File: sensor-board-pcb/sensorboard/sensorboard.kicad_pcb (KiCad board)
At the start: 2 copper layers, 19 parts, among them J1 TO_MOTHERBOARD, J10 PZT_08, J11 PZT_09, J12 PZT_10, J13 PZT_11, J14 PZT_12, J15 PZT_13, J16 PZT_14, J17 PZT_15, J2 PZT_00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

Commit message: board
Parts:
- moved J4 255.7 mm to (113.0, 129.0)
- moved J3 252.5 mm to (113.0, 119.2)
- moved J2 249.8 mm to (113.0, 108.7)
- moved J12 248.5 mm to (119.7, 148.4), turned to 90 degrees
- moved J6 246.3 mm to (113.0, 139.0)
- moved J13 242.6 mm to (130.2, 148.2), turned to 90 degrees
- moved J17 235.1 mm to (139.0, 148.5), turned to 90 degrees
- moved J16 220.8 mm to (148.5, 148.3), turned to 90 degrees
- moved J15 206.8 mm to (158.0, 148.4), turned to 90 degrees
- moved J9 201.3 mm to (176.0, 118.0)
- moved J8 199.5 mm to (176.0, 108.0)
- moved J7 198.1 mm to (176.0, 98.5)
- moved J14 194.1 mm to (166.2, 148.5), turned to 90 degrees
- moved J11 189.4 mm to (176.0, 139.0)
- moved J10 187.1 mm to (176.0, 128.5)
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
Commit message: routing fixed
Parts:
- moved J12 94.0 mm to (170.0, 69.0), turned to 0 degrees
- moved J9 91.2 mm to (110.0, 55.0)
- moved J13 82.4 mm to (170.0, 76.0), turned to 0 degrees
- moved J8 80.4 mm to (110.0, 62.0)
- moved J11 77.2 mm to (170.0, 62.0)
- moved J10 73.7 mm to (170.0, 55.0)
- moved J7 72.3 mm to (110.0, 69.0)
- moved J14 65.6 mm to (170.0, 83.0), turned to 0 degrees
- moved J6 63.0 mm to (110.0, 76.0)
- moved J15 59.6 mm to (170.0, 90.0), turned to 0 degrees
- moved J16 55.6 mm to (170.0, 97.0), turned to 0 degrees
- moved J17 54.2 mm to (170.0, 104.0), turned to 0 degrees
- moved J4 39.1 mm to (110.0, 90.0)
- moved J1 36.1 mm to (128.0, 48.0)
- moved U1 24.3 mm to (140.0, 80.0)
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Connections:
- J1 pad 8: unconnected-(J1-Pin_8-Pad8) -> +5V
- U1 pad 1: unconnected-(U1-COM-Pad1) -> ANALOG_COM
- U1 pad 10: DB_S2 -> DB_S0
- U1 pad 12: unconnected-(U1-GND-Pad12) -> GND
- U1 pad 13: unconnected-(U1-S3-Pad13) -> DB_S3
- U1 pad 14: DB_S0 -> DB_S2
- U1 pad 15: unconnected-(U1-~{E}-Pad15) -> DB_EN
- U1 pad 16: unconnected-(U1-I15-Pad16) -> PZT_15_P
- U1 pad 17: PZT_00_P -> PZT_14_P
- U1 pad 18: PZT_01_P -> PZT_13_P
- U1 pad 19: PZT_02_P -> PZT_12_P
- U1 pad 20: PZT_03_P -> PZT_11_P
- U1 pad 21: PZT_04_P -> PZT_10_P
- U1 pad 22: PZT_05_P -> PZT_09_P
- U1 pad 23: PZT_06_P -> PZT_08_P
- U1 pad 24: unconnected-(U1-VCC-Pad24) -> +5V
- U1 pad 3: PZT_08_P -> PZT_06_P
- U1 pad 4: PZT_09_P -> PZT_05_P
- U1 pad 5: PZT_10_P -> PZT_04_P
- U1 pad 6: PZT_11_P -> PZT_03_P
- U1 pad 7: PZT_12_P -> PZT_02_P
- U1 pad 8: PZT_13_P -> PZT_01_P
- U1 pad 9: PZT_14_P -> PZT_00_P
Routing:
- net GND: track 0.00 -> 351.7 mm, vias 0 -> 2
- net DB_S0: track 0.00 -> 42.7 mm, vias 0 -> 1
- net DB_S1: track 0.00 -> 41.6 mm, vias 0 -> 1
- net DB_S3: track 0.00 -> 40.4 mm, vias 0 -> 1
- net DB_S2: track 0.00 -> 39.5 mm, vias 0 -> 1
- net DB_EN: track 0.00 -> 37.8 mm, vias 0 -> 1
- net PZT_15_P: track 0.00 -> 34.5 mm
- net PZT_00_P: track 0.00 -> 34.5 mm
- net PZT_14_P: track 0.00 -> 30.9 mm
- net PZT_01_P: track 0.00 -> 30.9 mm
- net PZT_08_P: track 0.00 -> 30.4 mm
- net PZT_07_P: track 0.00 -> 30.4 mm
- net +5V: track 0.00 -> 28.9 mm, vias 0 -> 1
- net PZT_13_P: track 0.00 -> 28.0 mm
- net PZT_02_P: track 0.00 -> 28.0 mm
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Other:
- board outline added: 80 x 72 mm
- board text added: "16-PZT SENSORBOARD"
- board text added: "TO MOTHERBOARD"

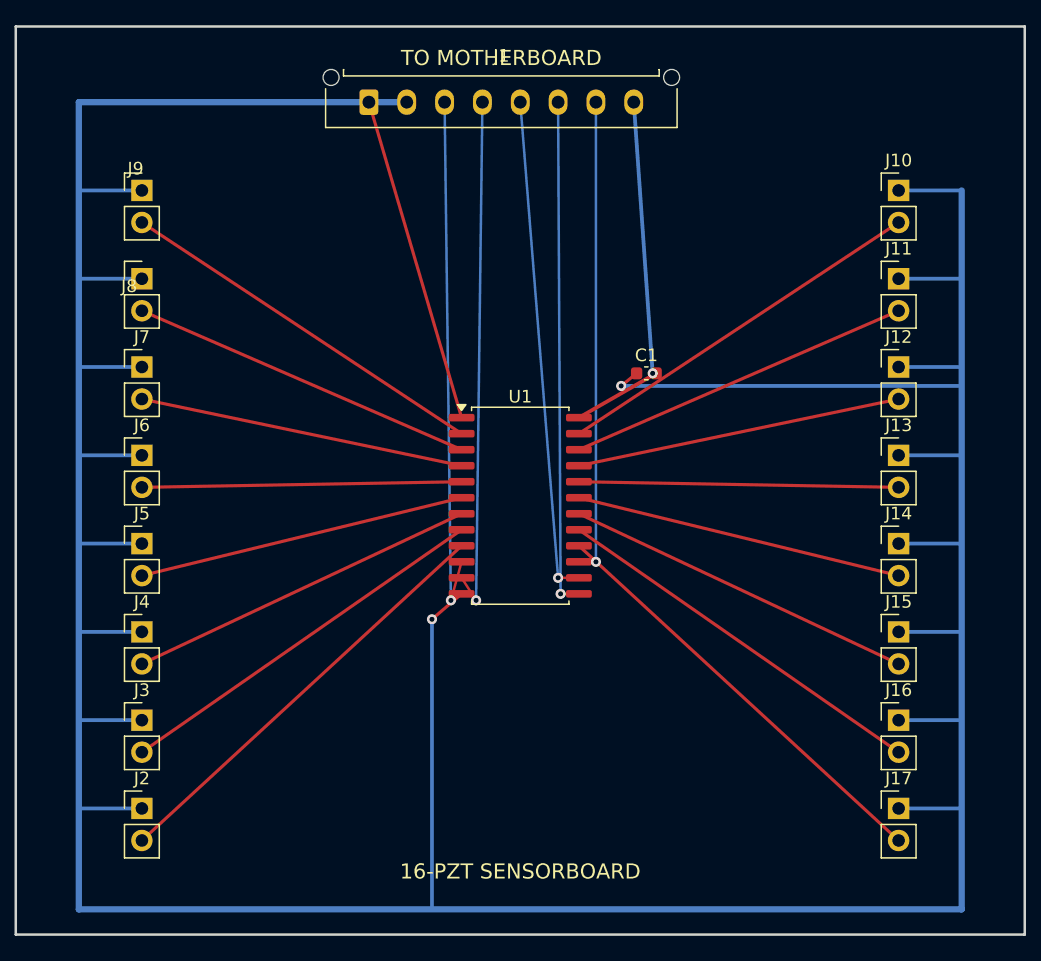
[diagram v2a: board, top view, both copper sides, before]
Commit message: fixed erc and drc issues, fixing routing
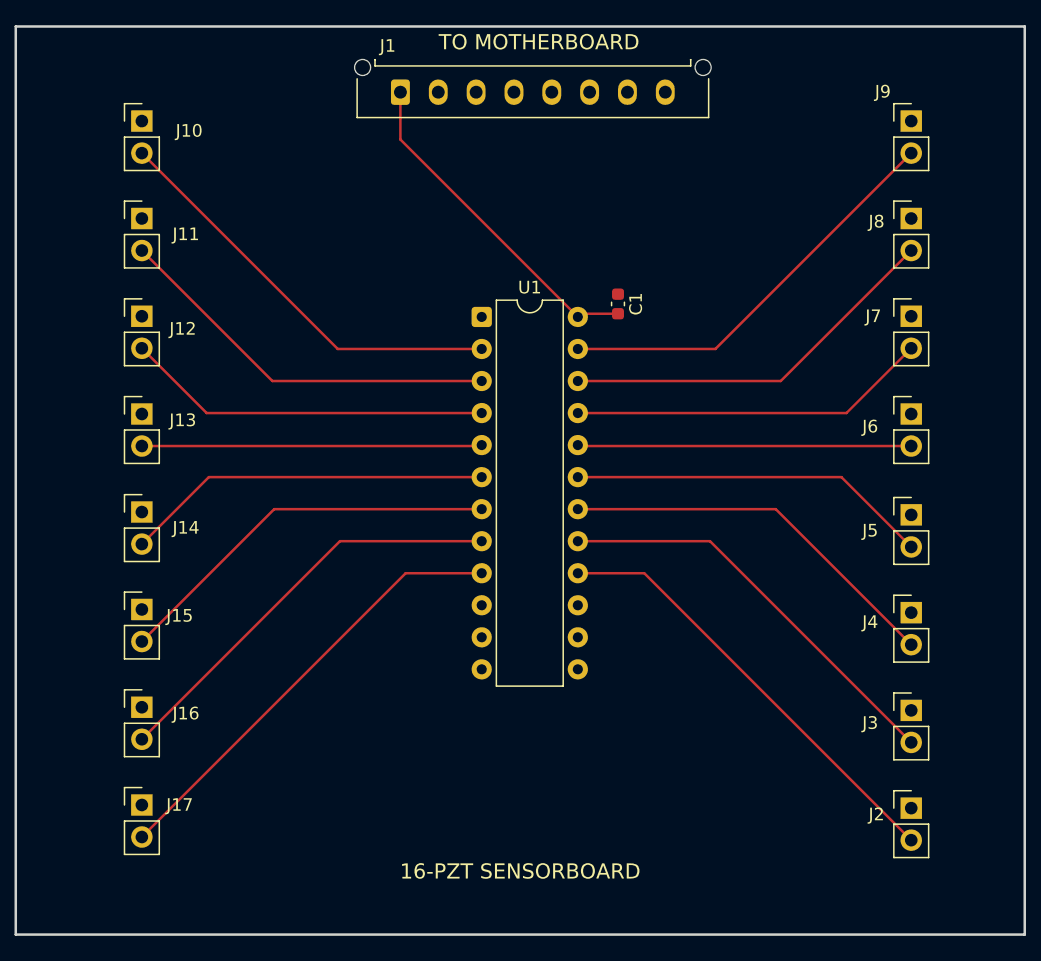
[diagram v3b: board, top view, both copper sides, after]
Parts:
- U1: footprint Package_SO:SOIC-24W_7.5x15.4mm_P1.27mm -> Package_DIP:DIP-24_W7.62mm
- moved J9 61.2 mm to (171.0, 49.5)
- moved J8 61.2 mm to (171.0, 57.2)
- moved J7 61.1 mm to (171.0, 65.0)
- moved J6 61.1 mm to (171.0, 72.7)
- moved J5 61.0 mm to (171.0, 80.7)
- moved J4 61.0 mm to (171.0, 88.5)
- moved J3 61.0 mm to (171.0, 96.2)
- moved J2 61.0 mm to (171.0, 104.0)
- moved J10 60.3 mm to (110.0, 49.5)
- moved J11 60.2 mm to (110.0, 57.2)
- moved J12 60.1 mm to (110.0, 65.0)
- moved J13 60.1 mm to (110.0, 72.7)
- moved J14 60.1 mm to (110.0, 80.5)
- moved J15 60.0 mm to (110.0, 88.2)
- moved J16 60.0 mm to (110.0, 96.0)
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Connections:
- J1 pad 1: ANALOG_COM -> +5V
- J1 pad 2: GND -> ANALOG_COM
- J1 pad 3: DB_S0 -> GND
- J1 pad 4: DB_S1 -> DB_S0
- J1 pad 5: DB_S2 -> DB_S1
- J1 pad 6: DB_S3 -> DB_S2
- J1 pad 7: DB_EN -> DB_S3
- J1 pad 8: +5V -> DB_EN
- U1 pad 1: ANALOG_COM -> DB_EN
- U1 pad 10: DB_S0 -> DB_S3
- U1 pad 11: DB_S1 -> DB_S0
- U1 pad 13: DB_S3 -> DB_S2
- U1 pad 14: DB_S2 -> DB_S1
- U1 pad 15: DB_EN -> ANALOG_COM
- U1 pad 16: PZT_15_P -> PZT_00_P
- U1 pad 17: PZT_14_P -> PZT_01_P
- U1 pad 18: PZT_13_P -> PZT_02_P
- U1 pad 19: PZT_12_P -> PZT_03_P
- U1 pad 2: PZT_07_P -> PZT_08_P
- U1 pad 20: PZT_11_P -> PZT_04_P
- U1 pad 21: PZT_10_P -> PZT_05_P
- U1 pad 22: PZT_09_P -> PZT_06_P
- U1 pad 23: PZT_08_P -> PZT_07_P
- U1 pad 3: PZT_06_P -> PZT_09_P
- U1 pad 4: PZT_05_P -> PZT_10_P
- U1 pad 5: PZT_04_P -> PZT_11_P
- U1 pad 6: PZT_03_P -> PZT_12_P
- U1 pad 7: PZT_02_P -> PZT_13_P
- U1 pad 8: PZT_01_P -> PZT_14_P
- U1 pad 9: PZT_00_P -> PZT_15_P
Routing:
- net GND: track 351.7 -> 0.00 mm, vias 2 -> 0
- net DB_S0: track 42.7 -> 0.00 mm, vias 1 -> 0
- net DB_S1: track 41.6 -> 0.00 mm, vias 1 -> 0
- net DB_S3: track 40.4 -> 0.00 mm, vias 1 -> 0
- net DB_S2: track 39.5 -> 0.00 mm, vias 1 -> 0
- net DB_EN: track 37.8 -> 0.00 mm, vias 1 -> 0
- net ANALOG_COM: track 26.1 -> 0.00 mm
- net PZT_09_P: track 27.6 -> 31.2 mm
- net PZT_13_P: track 28.0 -> 31.3 mm
- net PZT_10_P: track 25.9 -> 29.1 mm
- net PZT_06_P: track 27.6 -> 30.7 mm
- net PZT_12_P: track 26.1 -> 29.1 mm
- net PZT_08_P: track 30.4 -> 33.4 mm
- net PZT_02_P: track 28.0 -> 30.9 mm
- net PZT_05_P: track 25.9 -> 28.6 mm
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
